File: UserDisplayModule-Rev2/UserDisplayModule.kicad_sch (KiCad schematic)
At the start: 16 parts, among them J1 RJ45_Shielded, U8 LM7805_TO220

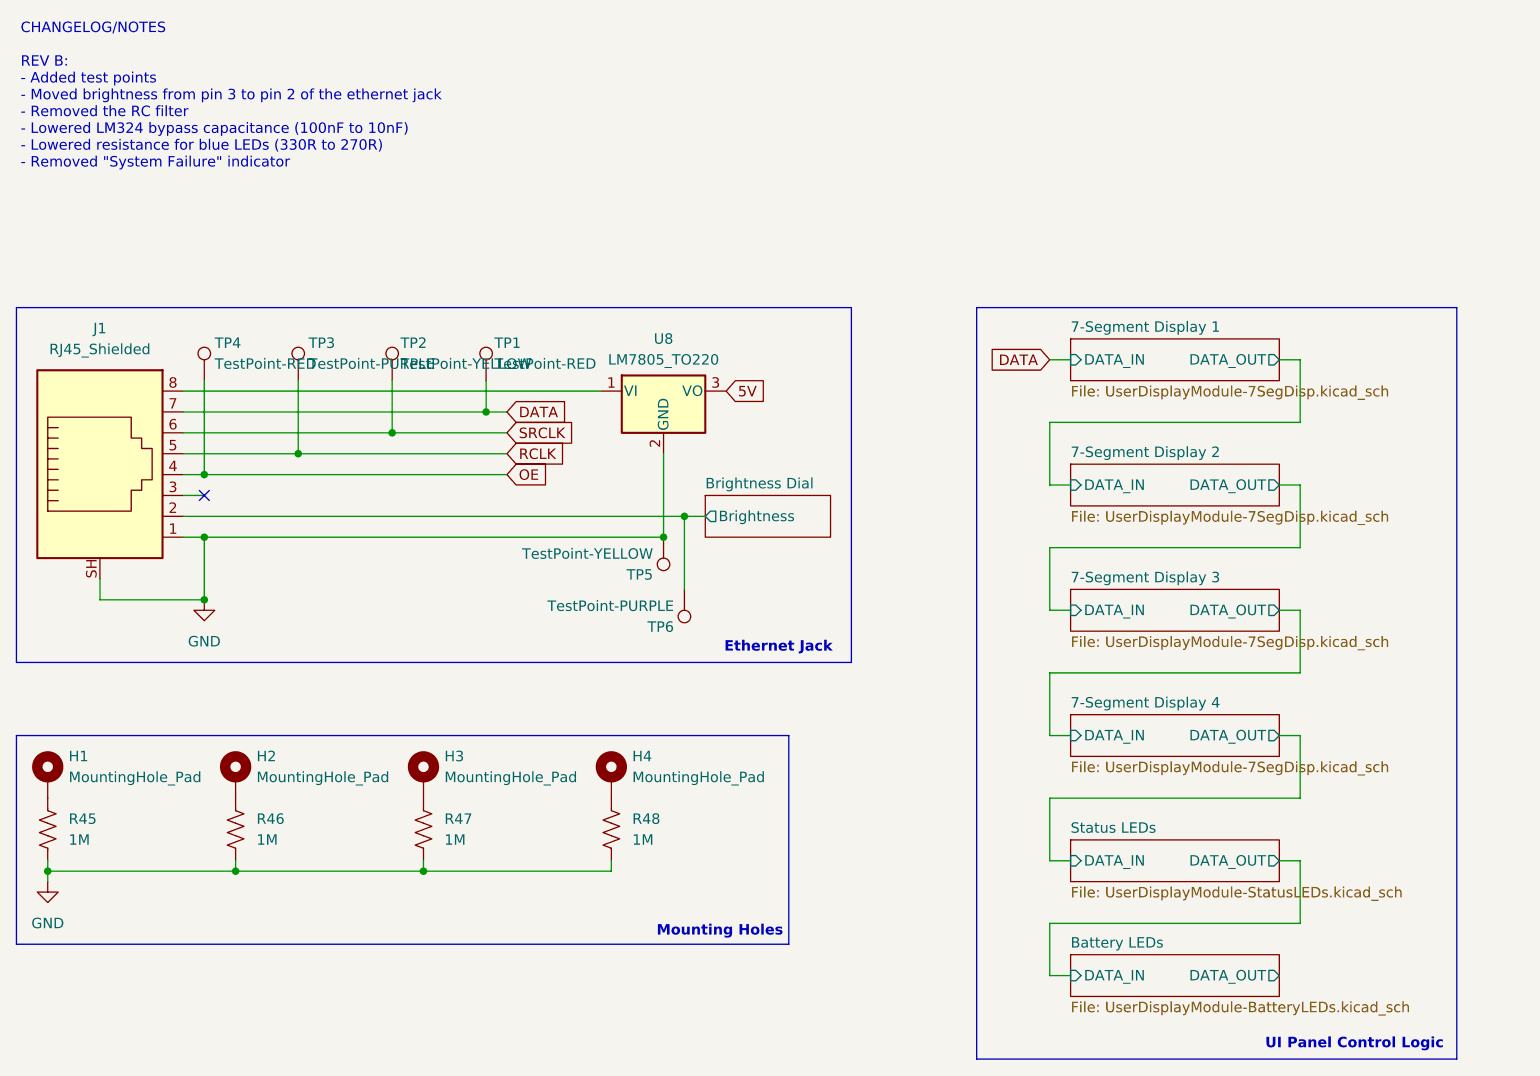
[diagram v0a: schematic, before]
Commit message: more changes: ldo bypass + grounding op amp
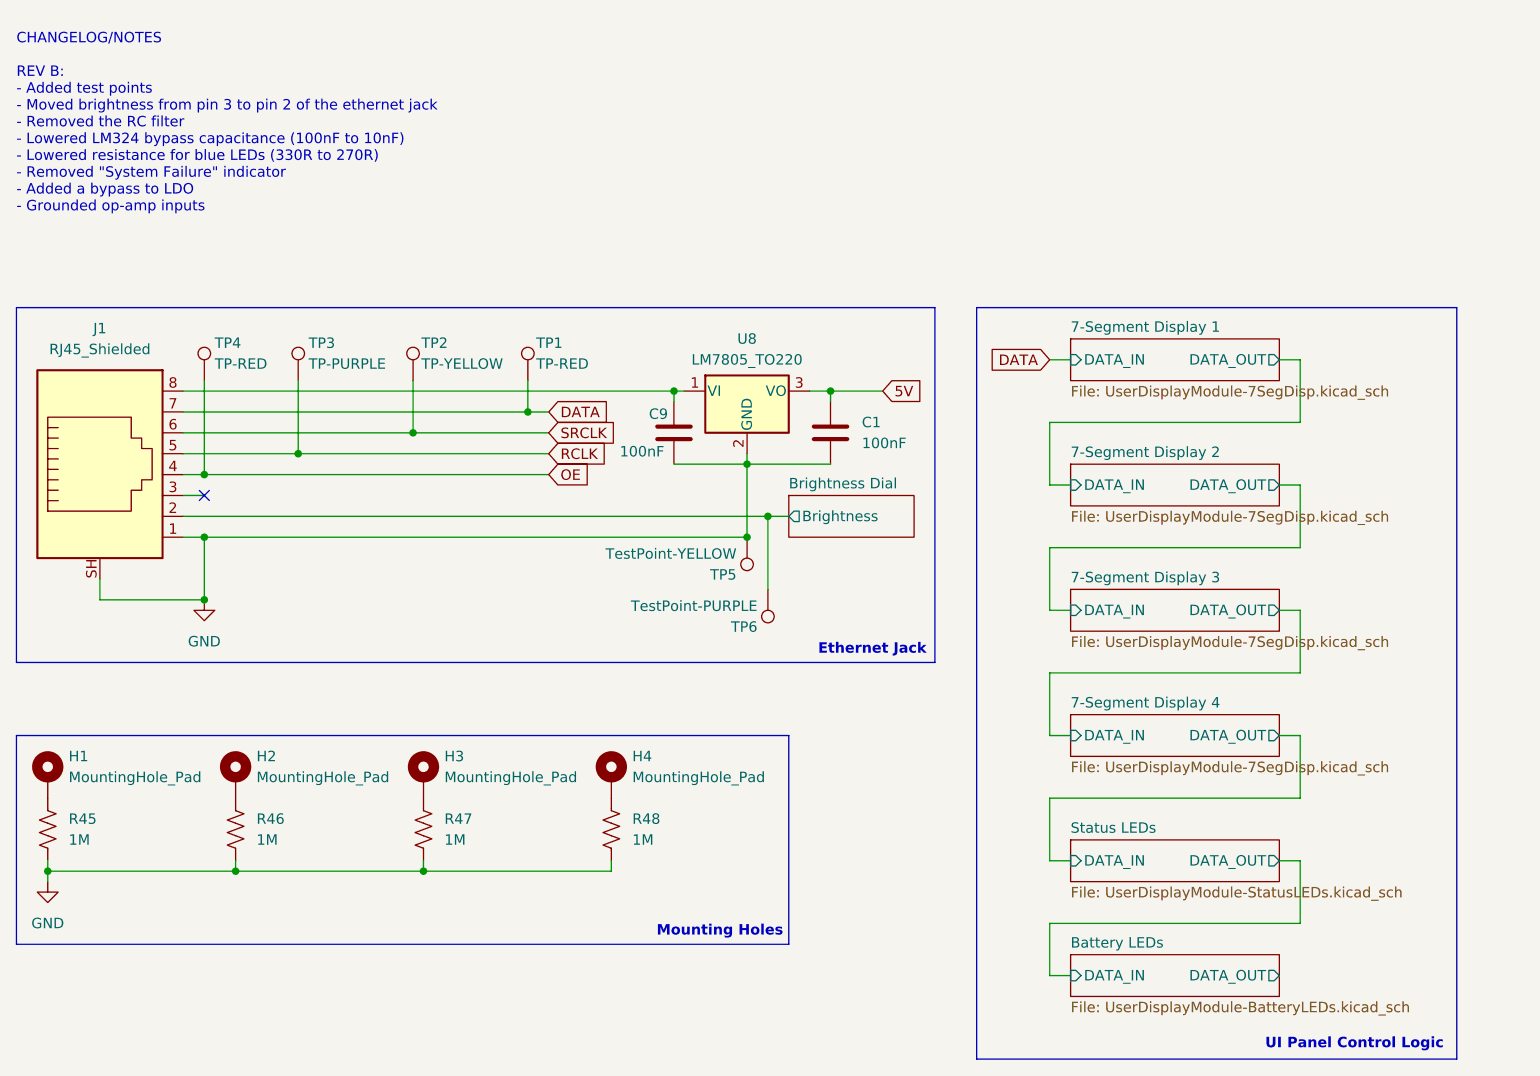
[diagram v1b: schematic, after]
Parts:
- added C1, C9: 100nF, Capacitor_SMD:C_0805_2012Metric, symbol Device:C
- TP1, TP4: value TestPoint-RED -> TP-RED
- TP2: value TestPoint-YELLOW -> TP-YELLOW
- TP3: value TestPoint-PURPLE -> TP-PURPLE
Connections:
- net 5V: now also C1.1
- net GND: now also C1.2, C9.2
- net at J1.8, U8.1 (VI): now also C9.1
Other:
- note added: "CHANGELOG/NOTES REV B: - Added test points - Moved brightness from pin 3 to pin 2 of the ethernet jack - Removed the RC filter - Lowered LM324 bypass capacitance (100nF to 10nF) - Lowered resistance for blue LEDs (330R to 270R) - Removed "System Failure" indicator - Added a bypass to LDO - Grounded op-amp inputs"
- note removed: "CHANGELOG/NOTES REV B: - Added test points - Moved brightness from pin 3 to pin 2 of the ethernet jack - Removed the RC filter - Lowered LM324 bypass capacitance (100nF to 10nF) - Lowered resistance for blue LEDs (330R to 270R) - Removed "System Failure" indicator"
- moved on the sheet: TP1, TP2, TP5, TP6, U8
